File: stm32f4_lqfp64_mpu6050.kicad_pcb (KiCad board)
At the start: 4 copper layers, 130 x 100 mm, 156 parts, among them M5 ALIS-CUSTOM-PARTS_POWERPADS, P1 CONN_01X08, P2 CONN_02X08, Q5 BSS138, Q6 CRYSTAL_50X32, U1 STM32F405R, U2 MPU6050, U3 LP2985LV, U4 LP2985LV, U5 W25Q80BV, U6 LM1881, U7 TS5A3160, U8 TS5A3160, X1 CON-JST_SM04B-SRSS-TB, X2 CON-JST_SM04B-SRSS-TB, X4 CON-JST_SM04B-SRSS-TB

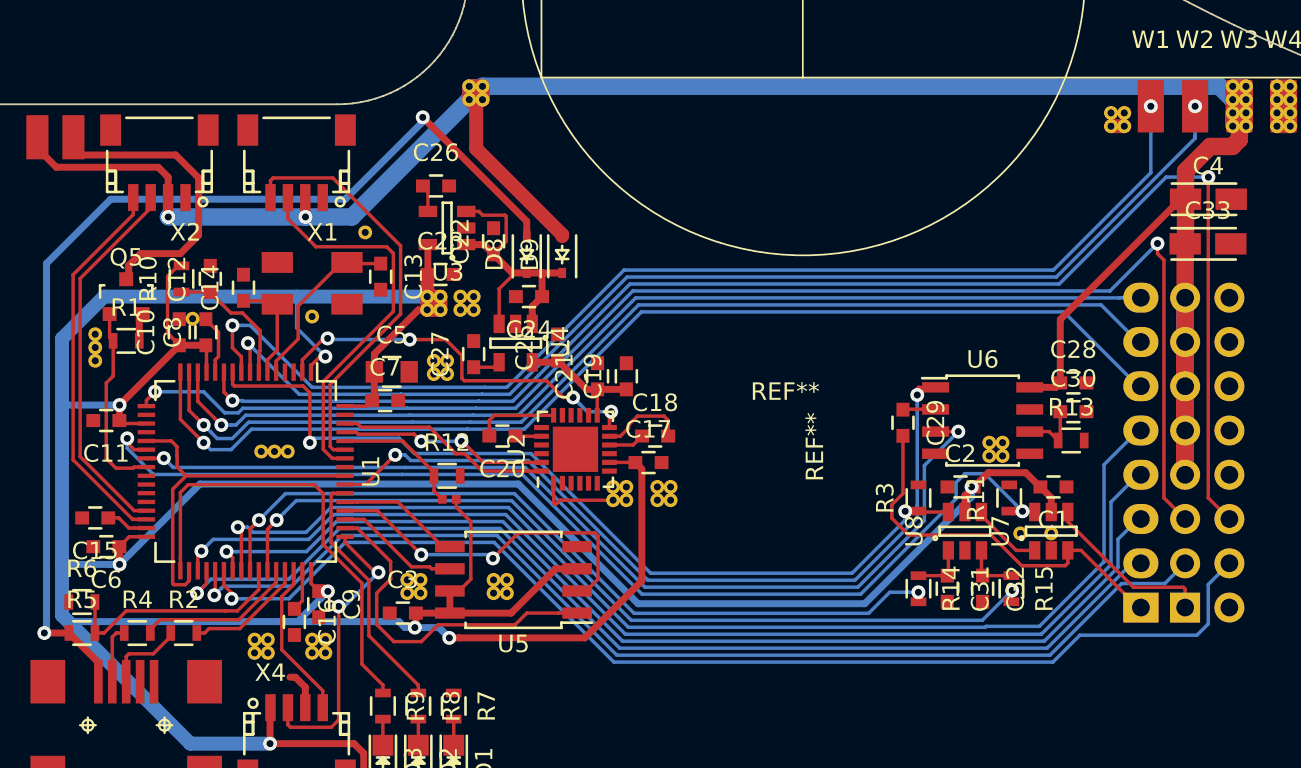
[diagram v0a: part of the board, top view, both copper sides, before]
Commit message: second pass routing complete
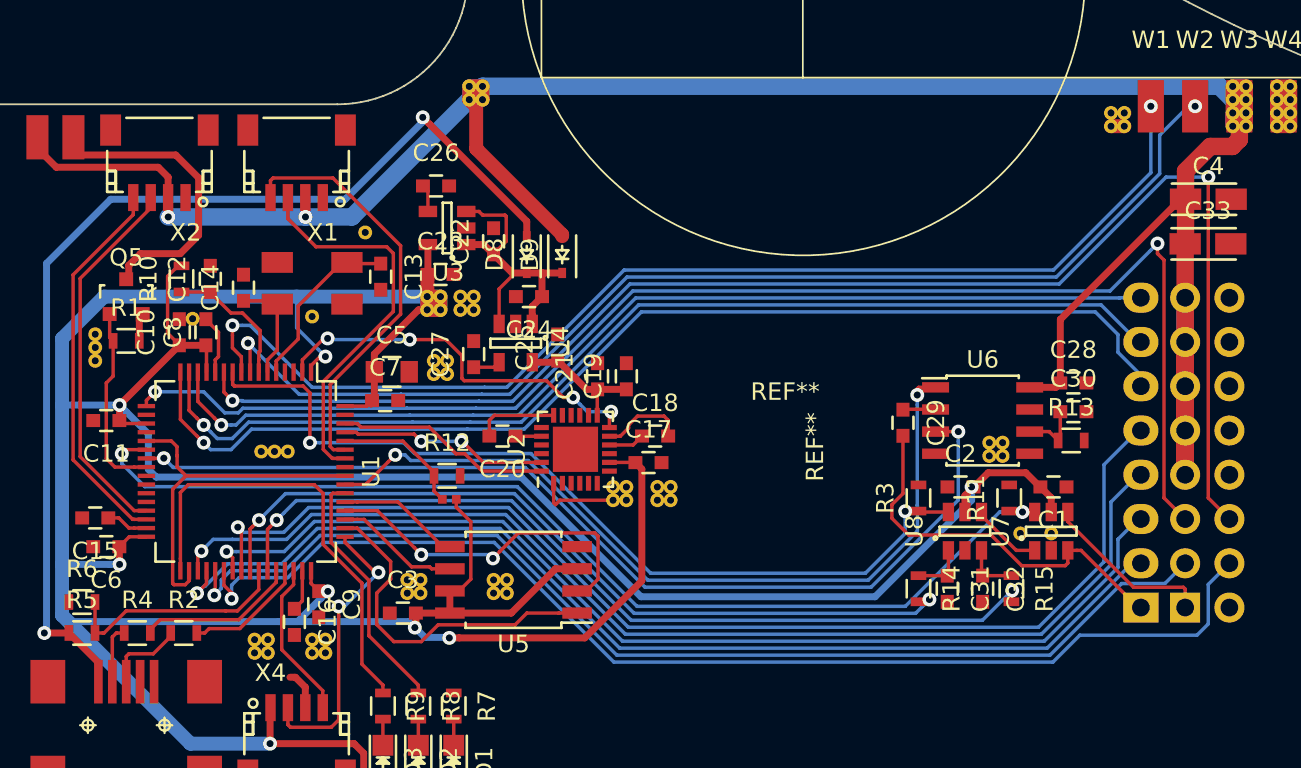
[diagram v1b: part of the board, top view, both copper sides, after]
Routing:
- net 3.3V: track 246.9 -> 250.9 mm
- net BW_MASK: track 63.4 -> 60.9 mm
- net TIM5_CH3: track 63.6 -> 64.6 mm
- net B_PWM: track 45.5 -> 46.1 mm

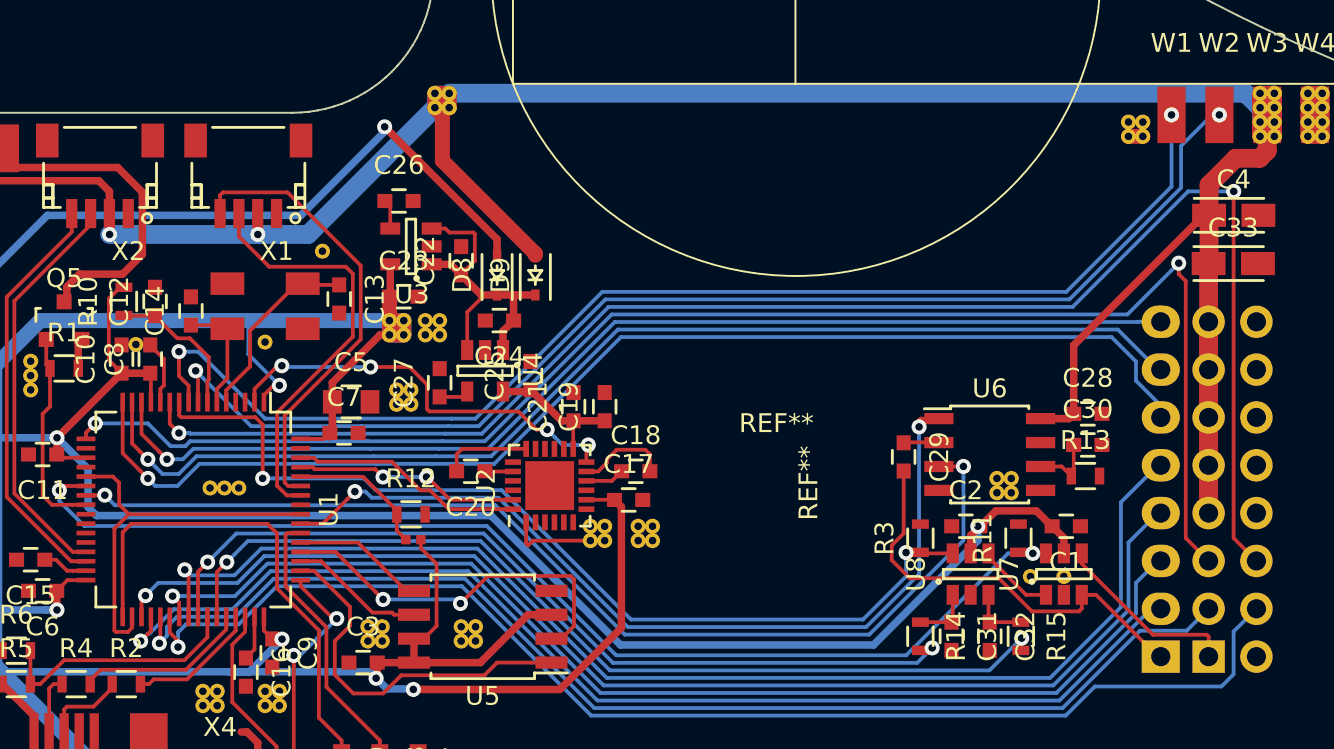
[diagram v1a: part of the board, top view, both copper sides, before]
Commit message: re-routed upper three video signals
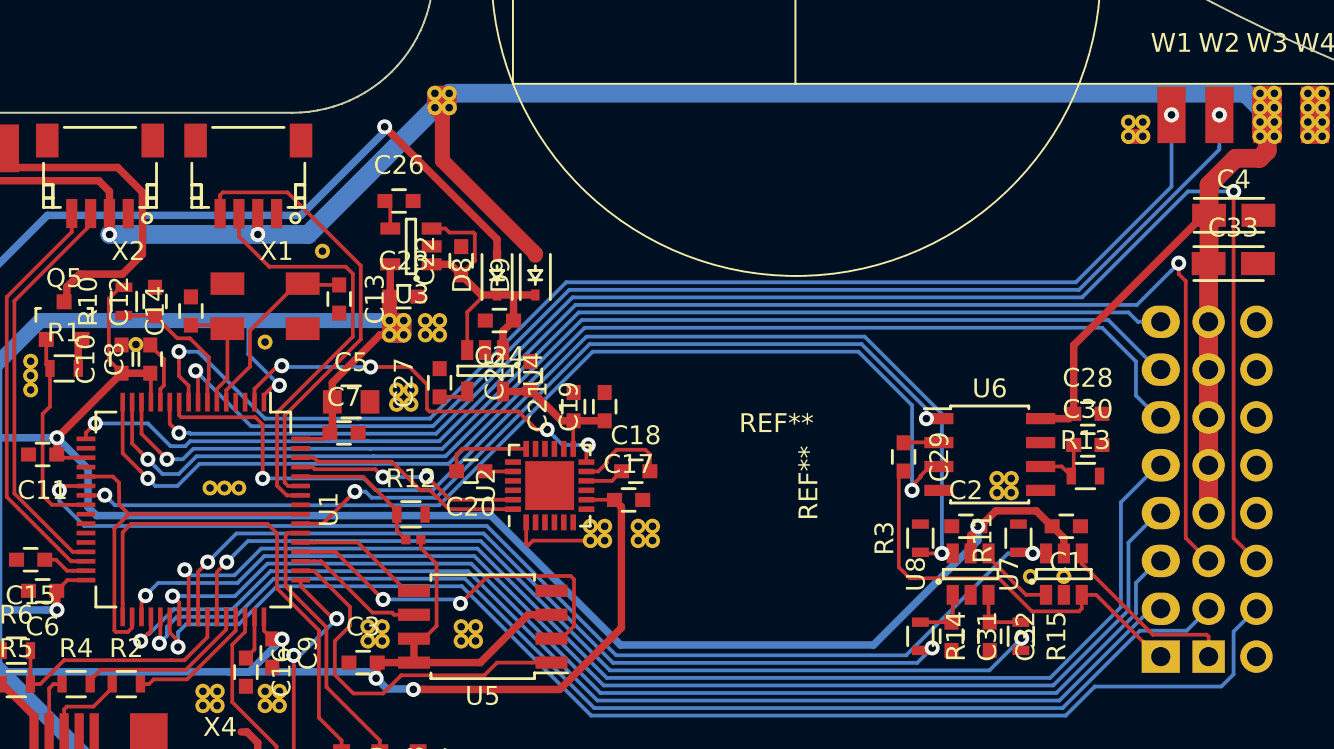
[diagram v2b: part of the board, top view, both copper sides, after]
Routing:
- net BW_LEVEL: track 50.2 -> 58.7 mm
- net HSYNC_CAPT: track 47.0 -> 40.0 mm
- net VSYNC_EXTI: track 57.0 -> 55.3 mm

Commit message: looks better than the rcexplorer naze32
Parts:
- moved X4 0.25 mm to (116.1, 121.8)
- moved ? 0.13 mm to (114.4, 115.8)
- moved ? 0.13 mm to (113.7, 116.6)
- moved ? 0.13 mm to (113.7, 115.8)
- moved ? 0.13 mm to (114.4, 116.6)
- moved ? 0.13 mm to (117.0, 115.8)
- moved ? 0.13 mm to (117.0, 116.6)
- moved ? 0.13 mm to (117.7, 116.6)
- moved ? 0.13 mm to (117.7, 115.8)
- moved REF** 0.13 mm to (145.3, 104.8)
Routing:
- net TIM8_CH3: track 61.1 -> 62.7 mm
- net TIM12_CH1/PPM: track 64.7 -> 65.6 mm
- net BW_MASK: track 60.9 -> 60.3 mm
- net TIM8_CH2/FRSKY_RSSI/DSM: track 67.4 -> 66.7 mm

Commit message: looks better than the rcexplorer naze32
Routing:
- net VBAT: track 171.4 -> 170.3 mm
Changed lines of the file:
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@@
     (thickness 1.6)
     (drawings 2)
-    (tracks 846)
+    (tracks 843)
     (zones 0)
     (modules 156)
@@
   (segment (start 107.049 98.552) (end 107.049 97.21276) (width 0.4) (layer Top) (net 1))
   (segment (start 107.049 97.21276) (end 107.249 97.01276) (width 0.4) (layer Top) (net 1))
-  (segment (start 169.029998 83.939998) (end 169.022996 83.947) (width 1) (layer Bottom) (net 2))
   (segment (start 169.022996 83.947) (end 126.746 83.947) (width 1) (layer Bottom) (net 2))
   (segment (start 126.746 83.947) (end 126.383999 84.309001) (width 1) (layer Bottom) (net 2))
@@
   (segment (start 170.561 83.947) (end 170.561 86.233) (width 1) (layer Bottom) (net 2))
   (segment (start 170.561 83.947) (end 169.037 83.947) (width 1) (layer Bottom) (net 2))
-  (segment (start 169.037 83.947) (end 169.029998 83.939998) (width 1) (layer Bottom) (net 2))
   (segment (start 167.092 90.424) (end 164.084 90.424) (width 0.4) (layer Top) (net 2))
   (segment (start 164.084 90.424) (end 159.905 94.603) (width 0.4) (layer Top) (net 2))
@@
   (segment (start 170.18 87.376) (end 170.18 85.217) (width 1) (layer Top) (net 2))
   (segment (start 167.755999 88.145001) (end 169.410999 88.145001) (width 1) (layer Top) (net 2))
-  (segment (start 169.799 84.709) (end 169.029998 83.939998) (width 1) (layer Bottom) (net 2))
   (segment (start 167.0685 103.6955) (end 167.0685 106.2355) (width 1) (layer Top) (net 2))
   (segment (start 167.0685 101.1555) (end 167.0685 103.6955) (width 1) (layer Top) (net 2))
@@
   (via (at 116.84 104.394) (size 0.8) (drill 0.4) (layers Top Bottom) (net 42))
   (segment (start 151.82 108.374) (end 151.765 108.319) (width 0.2) (layer Top) (net 42))
+  (segment (start 112.395001 101.981) (end 112.522 101.981) (width 0.2) (layer Bottom) (net 43))
+  (segment (start 112.522 101.981) (end 112.560022 102.019022) (width 0.2) (layer Bottom) (net 43))
+  (segment (start 133.162078 94.907022) (end 160.224378 94.907022) (width 0.2) (layer Bottom) (net 43))
+  (segment (start 112.560022 102.019022) (end 122.231836 102.019022) (width 0.2) (layer Bottom) (net 43))
+  (segment (start 122.233065 102.017793) (end 126.051307 102.017793) (width 0.2) (layer Bottom) (net 43))
   (segment (start 122.231836 102.019022) (end 122.233065 102.017793) (width 0.2) (layer Bottom) (net 43))
-  (segment (start 165.836389 89.295011) (end 167.848421 89.295011) (width 0.2) (layer Bottom) (net 43))
+  (segment (start 167.848421 89.295011) (end 168.414106 89.295011) (width 0.2) (layer Bottom) (net 43))
   (segment (start 126.051307 102.017793) (end 133.162078 94.907022) (width 0.2) (layer Bottom) (net 43))
-  (segment (start 122.233065 102.017793) (end 126.051307 102.017793) (width 0.2) (layer Bottom) (net 43))
-  (segment (start 133.162078 94.907022) (end 160.224378 94.907022) (width 0.2) (layer Bottom) (net 43))
-  (segment (start 112.960686 101.981) (end 112.998708 102.019022) (width 0.2) (layer Bottom) (net 43))
+  (segment (start 165.836389 89.295011) (end 167.848421 89.295011) (width 0.2) (layer Bottom) (net 43))
   (segment (start 160.224378 94.907022) (end 165.836389 89.295011) (width 0.2) (layer Bottom) (net 43))
-  (segment (start 112.998708 102.019022) (end 122.231836 102.019022) (width 0.2) (layer Bottom) (net 43))
-  (segment (start 167.848421 89.295011) (end 168.414106 89.295011) (width 0.2) (layer Bottom) (net 43))
-  (segment (start 112.395001 101.981) (end 112.960686 101.981) (width 0.2) (layer Bottom) (net 43))
   (segment (start 168.414106 89.860696) (end 168.414106 89.295011) (width 0.2) (layer Top) (net 43))
   (segment (start 168.394899 89.879903) (end 168.414106 89.860696) (width 0.2) (layer Top) (net 43))
@@
   (segment (start 121.892 107.795) (end 119.557 107.795) (width 0.2) (layer Top) (net 61))
   (segment (start 119.557 107.795) (end 118.857 107.795) (width 0.2) (layer Top) (net 61))
-  (segment (start 122.627329 105.417867) (end 126.045433 105.417867) (width 0.2) (layer Bottom) (net 62))
-  (segment (start 152.08401 100.70671) (end 152.08401 101.218998) (width 0.2) (layer Bottom) (net 62))
-  (segment (start 134.156212 97.307088) (end 148.684388 97.307088) (width 0.2) (layer Bottom) (net 62))
+  (segment (start 121.737787 105.09401) (end 121.737787 105.100787) (width 0.2) (layer Bottom) (net 62))
+  (segment (start 121.737787 105.100787) (end 122.054867 105.417867) (width 0.2) (layer Bottom) (net 62))
+  (segment (start 122.054867 105.417867) (end 126.045433 105.417867) (width 0.2) (layer Bottom) (net 62))
   (segment (start 148.684388 97.307088) (end 152.08401 100.70671) (width 0.2) (layer Bottom) (net 62))
-  (segment (start 122.303472 105.09401) (end 122.627329 105.417867) (width 0.2) (layer Bottom) (net 62))
-  (segment (start 121.737787 105.09401) (end 122.303472 105.09401) (width 0.2) (layer Bottom) (net 62))
   (segment (start 126.045433 105.417867) (end 134.156212 97.307088) (width 0.2) (layer Bottom) (net 62))
+  (segment (start 134.156212 97.307088) (end 148.684388 97.307088) (width 0.2) (layer Bottom) (net 62))
+  (segment (start 152.08401 100.70671) (end 152.08401 101.218998) (width 0.2) (layer Bottom) (net 62))
   (segment (start 152.649695 101.218998) (end 152.08401 101.218998) (width 0.2) (layer Top) (net 62))
   (segment (start 152.748 101.219) (end 152.747998 101.218998) (width 0.2) (layer Top) (net 62))

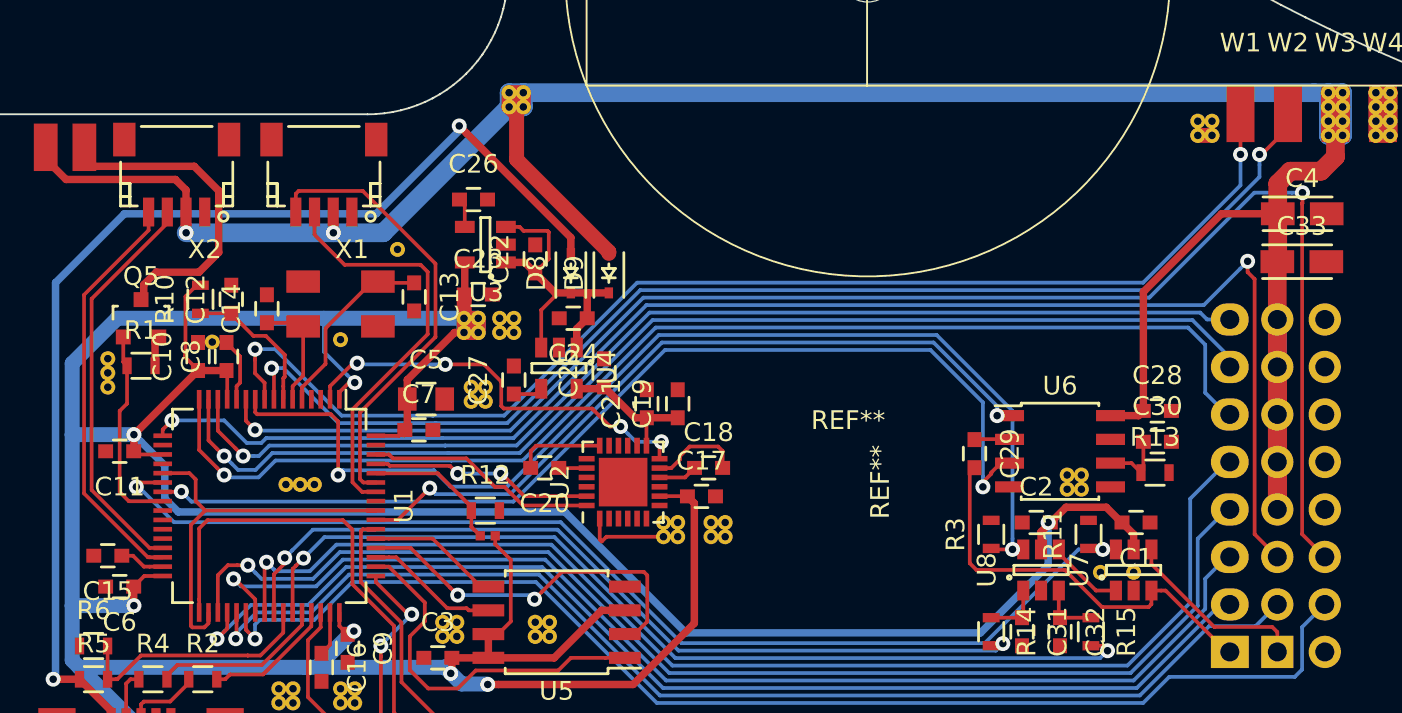
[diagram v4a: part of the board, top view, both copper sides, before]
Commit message: improved a few ground connections
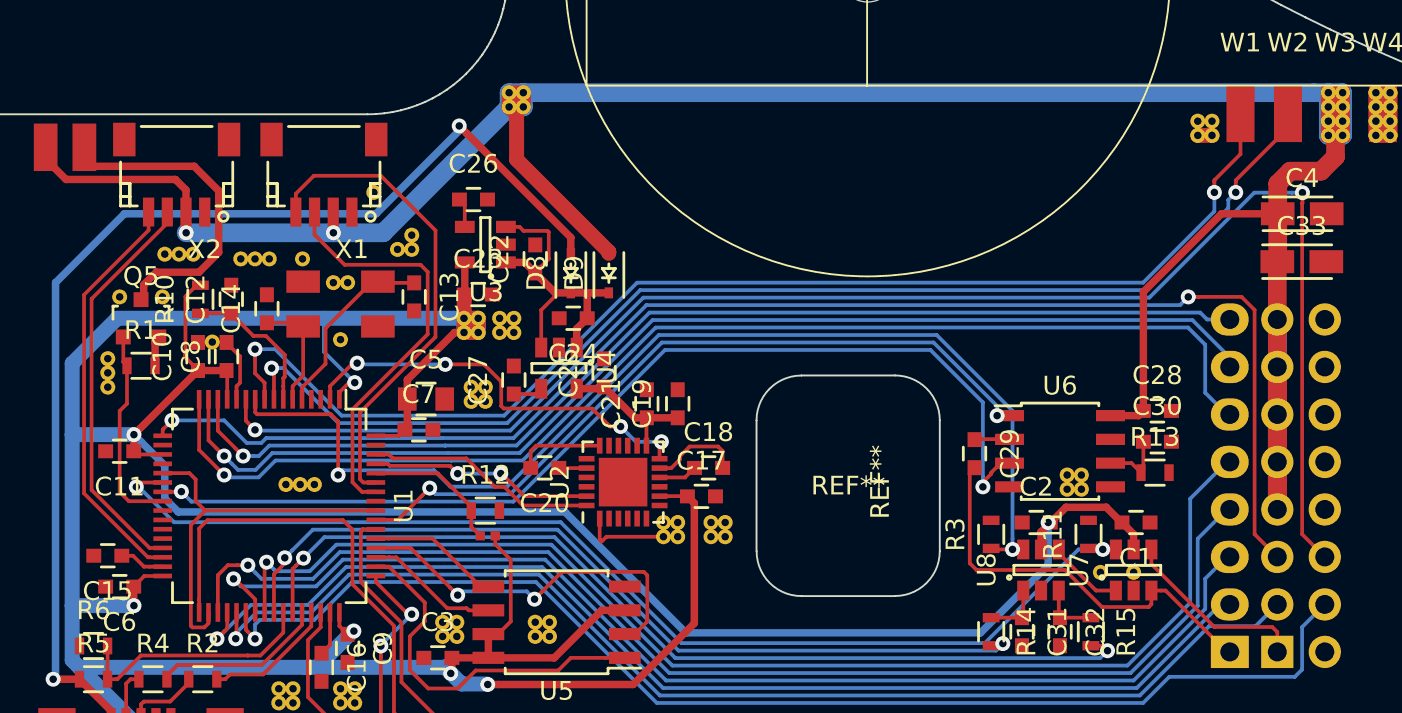
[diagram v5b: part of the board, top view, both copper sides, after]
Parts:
- added ?: , alis_parts:via_04, F.Cu at (107.4, 94.9)
- added ?: , alis_parts:via_04, F.Cu at (116.6, 94.1)
- added ?: , alis_parts:via_04, F.Cu at (117.3, 94.1)
- added ?: , alis_parts:via_04, F.Cu at (118.7, 89.3)
- added ?: , alis_parts:via_04, F.Cu at (120.8, 91.6)
- added ?: , alis_parts:via_04, F.Cu at (120.8, 92.3)
- added ?: , alis_parts:via_04, F.Cu at (105.2, 94.9)
- added ?: , alis_parts:via_04, F.Cu at (107.6, 92.6)
- added ?: , alis_parts:via_04, F.Cu at (108.3, 92.6)
- added ?: , alis_parts:via_04, F.Cu at (109.1, 92.6)
- added ?: , alis_parts:via_04, F.Cu at (111.6, 92.8)
- added ?: , alis_parts:via_04, F.Cu at (112.4, 92.8)
- added ?: , alis_parts:via_04, F.Cu at (113.2, 92.8)
- added ?: , alis_parts:via_04, F.Cu at (114.9, 92.8)
- REF**: value PositioningHole_1mm -> (none); footprint alis_parts:PositioningHole_1mm -> alis_parts:rectangular_hole_10x12mm
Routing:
- net TIM5_CH4: track 79.6 -> 76.7 mm
- net MAIN_RX/DSM: track 24.2 -> 26.0 mm
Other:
- board text added: "Alexander Tuxen 2016"
- board text added: "PPM Servo Back Left Right"
- board text added: "Vin Vout GND PWM7 PWM8 DSM PWM5 PWM6 ADC3"
- board text removed: "alibenpeng!"
